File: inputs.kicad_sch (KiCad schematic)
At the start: 56 parts, among them J2 Dual_Stereo_RCA_Jack, J3 Dual_Stereo_RCA_Jack, U1 TL072, U2 TL072

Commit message: Added decoupling and output caps
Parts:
- removed unit 3 of U1
- removed unit 3 of U2
- removed U?: TL072, symbol Amplifier_Operational:TL072
- gave numbers to parts that had none: 18

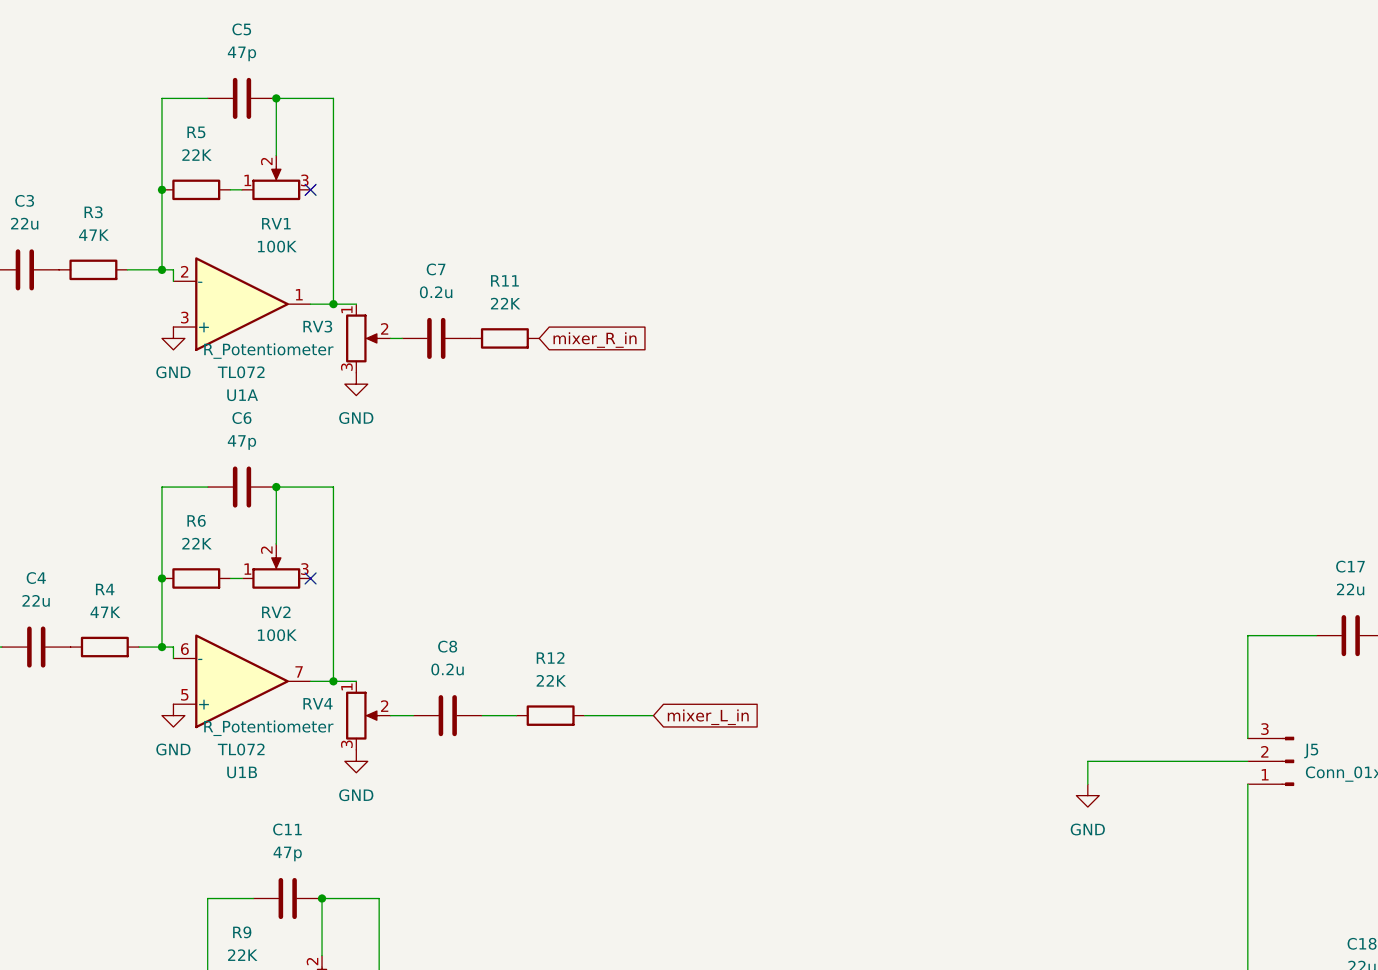
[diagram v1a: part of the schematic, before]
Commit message: Refactored and made modular inputs
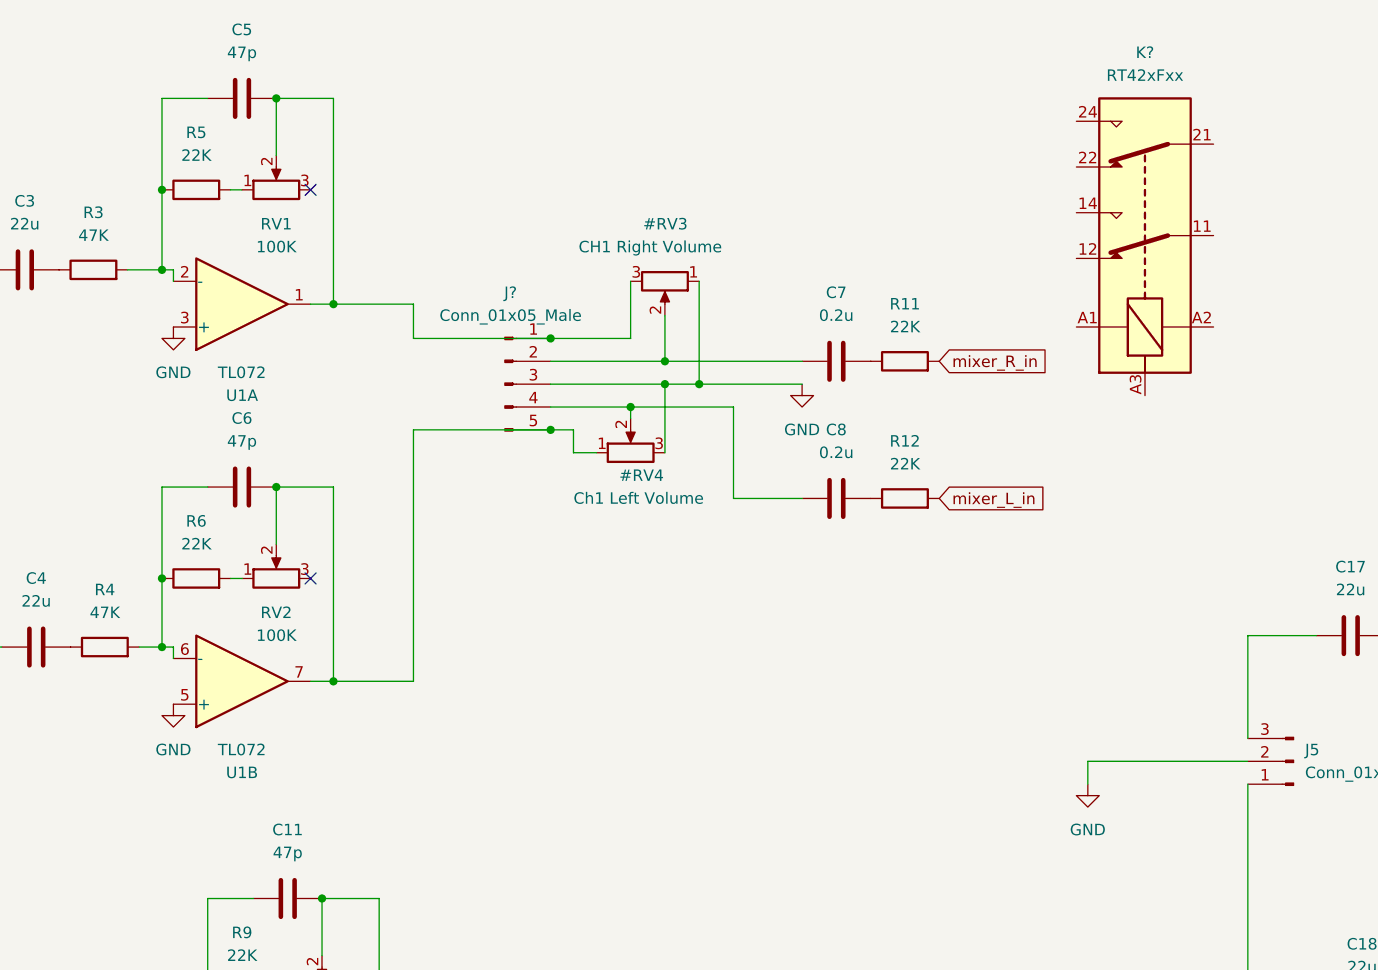
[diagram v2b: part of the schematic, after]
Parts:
- added J?: Conn_01x05_Male, symbol Connector:Conn_01x05_Male
- added K?: RT42xFxx, Relay_THT:Relay_DPDT_Schrack-RT2-FormC-Dual-Coil_RM5mm, symbol Relay:RT42xFxx
- #RV3: renamed from RV3; value R_Potentiometer -> CH1 Right Volume
- #RV4: renamed from RV4; value R_Potentiometer -> Ch1 Left Volume
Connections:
- net GND: now also #RV3.1, J?.3 (Pin_3); no longer #RV3.3
- net at C5.2, RV1.2, U1.1: now also #RV3.3, J?.1 (Pin_1); no longer #RV3.1
- net at #RV3.2, C7.1: now also J?.2 (Pin_2)
- net at #RV4.1, C6.2, RV2.2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: now also J?.5 (Pin_5)
- net at #RV4.2, C8.1: now also J?.4 (Pin_4)
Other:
- moved on the sheet: C7, C8, R11, R12
